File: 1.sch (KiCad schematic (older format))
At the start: 46 parts, among them J1 Micro_SD_Card, J10 BxI2C1, J11 I2C2, J2 USB_B_Micro, J3 Power, J4 SWD, J5 Protected, J6 SPI1, J7 ADC, J8 UART1, J9 SPI2, K1 NRST, K2 WKUP, K3 KPA0, U1 STM32F103C8Tx, U2 AMS1117-3.3, Y1 8MHz, Y2 32.768k

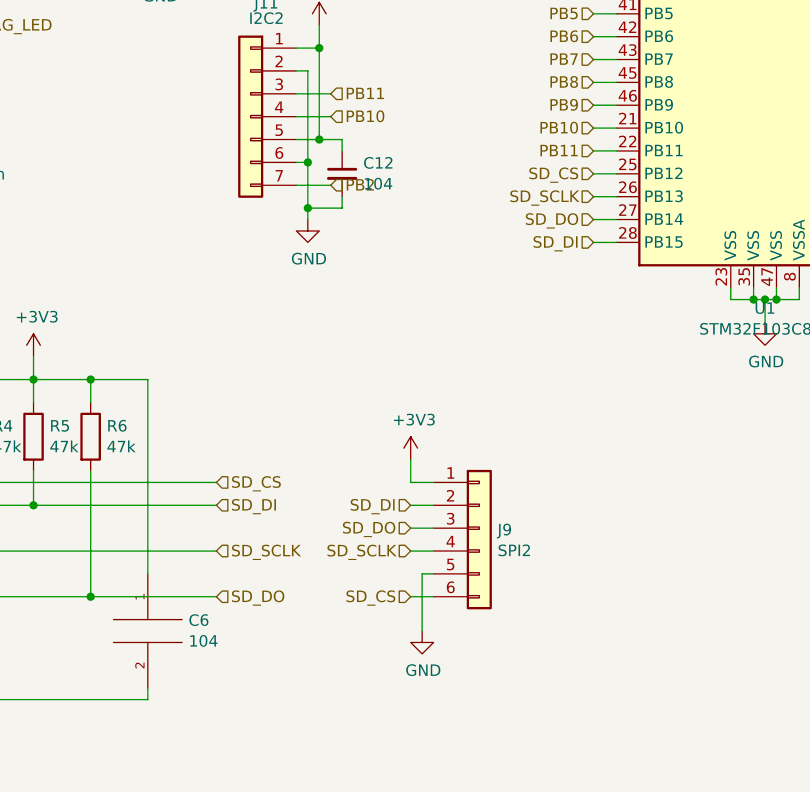
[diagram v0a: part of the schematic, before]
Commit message: rename label to PAxx/PBxx on 原理图
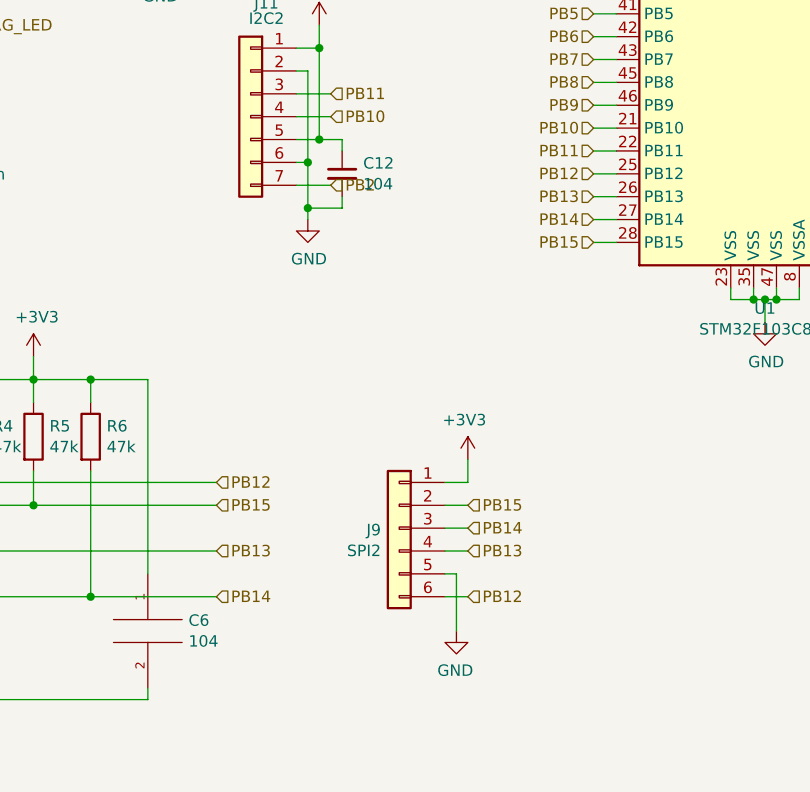
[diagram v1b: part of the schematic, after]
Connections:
- net SD_CS renamed PB12
- net SD_DI renamed PB15
- net SD_DO renamed PB14
- net SD_SCLK renamed PB13
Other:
- moved on the sheet: J9
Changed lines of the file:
@@
 	3000 6600 3800 6600
 Text HLabel 3800 6500 2    50   Input ~ 0
-SD_CS
+PB12
 Text HLabel 3800 6600 2    50   Input ~ 0
-SD_DI
+PB15
 Text HLabel 3800 6800 2    50   Input ~ 0
-SD_SCLK
+PB13
 Text HLabel 3800 7000 2    50   Input ~ 0
-SD_DO
+PB14
 $Comp
 L power:+3V3 #PWR0106
@@
 Wire Wire Line
 	5450 5150 5550 5150
-Text HLabel 5450 5250 0    50   Input ~ 0
-SD_SCLK
 Wire Wire Line
 	5450 5250 5550 5250
-Text HLabel 5450 5150 0    50   Input ~ 0
-SD_CS
 Wire Wire Line
 	5550 5350 5450 5350
@@
 	5450 5450 5550 5450
 Text HLabel 5450 5350 0    50   Input ~ 0
-SD_DO
+PB14
 Text HLabel 5450 5450 0    50   Input ~ 0
-SD_DI
+PB15
 Text HLabel 5450 2850 0    50   Input ~ 0
 NRST
@@
 	6950 2600 6950 2750
 Connection ~ 6450 2600
-Text HLabel 2750 4500 2    50   Input ~ 0
-RG_LED
 Wire Wire Line
 	10400 2700 10600 2700
@@
 L power:+3V3 #PWR0120
 U 1 1 61290385
-P 4650 6400
-F 0 "#PWR0120" H 4650 6250 50  0001 C CNN
-F 1 "+3V3" H 4665 6573 50  0000 C CNN
-F 2 "" H 4650 6400 50  0001 C CNN
-F 3 "" H 4650 6400 50  0001 C CNN
-	1    4650 6400
-	1    0    0    -1
-$EndComp
-Text HLabel 4650 7000 0    50   Input ~ 0
-SD_CS
-Wire Wire Line
-	4650 6500 4750 6500
-Wire Wire Line
-	4650 6400 4650 6500
-Wire Wire Line
-	4650 6600 4750 6600
-Wire Wire Line
-	4650 6700 4750 6700
-Wire Wire Line
-	4650 6800 4750 6800
-Text HLabel 4650 6600 0    50   Input ~ 0
-SD_DI
-Text HLabel 4650 6700 0    50   Input ~ 0
-SD_DO
-Text HLabel 4650 6800 0    50   Input ~ 0
-SD_SCLK
-Wire Wire Line
-	4700 6900 4700 7150
+P 4900 6400
+F 0 "#PWR0120" H 4900 6250 50  0001 C CNN
+F 1 "+3V3" H 4915 6573 50  0000 C CNN
+F 2 "" H 4900 6400 50  0001 C CNN
+F 3 "" H 4900 6400 50  0001 C CNN
+	1    4900 6400
+	-1   0    0    -1
+$EndComp
+Text HLabel 4900 7000 2    50   Input ~ 0
+PB12
+Wire Wire Line
+	4900 6500 4800 6500
+Wire Wire Line
+	4900 6400 4900 6500
+Wire Wire Line
+	4900 6600 4800 6600
+Wire Wire Line
+	4900 6700 4800 6700
+Wire Wire Line
+	4900 6800 4800 6800
+Text HLabel 4900 6600 2    50   Input ~ 0
+PB15
+Text HLabel 4900 6700 2    50   Input ~ 0
+PB14
+Text HLabel 4900 6800 2    50   Input ~ 0
+PB13
+Wire Wire Line
+	4850 6900 4850 7150
 $Comp
 L power:GND #PWR0124
 U 1 1 61009CA8
-P 4700 7150
-F 0 "#PWR0124" H 4700 6900 50  0001 C CNN
-F 1 "GND" H 4705 6977 50  0000 C CNN
-F 2 "" H 4700 7150 50  0001 C CNN
-F 3 "" H 4700 7150 50  0001 C CNN
-	1    4700 7150
-	1    0    0    -1
-$EndComp
-Wire Wire Line
-	4750 6900 4700 6900
-Wire Wire Line
-	4650 7000 4750 7000
+P 4850 7150
+F 0 "#PWR0124" H 4850 6900 50  0001 C CNN
+F 1 "GND" H 4855 6977 50  0000 C CNN
+F 2 "" H 4850 7150 50  0001 C CNN
+F 3 "" H 4850 7150 50  0001 C CNN
+	1    4850 7150
+	-1   0    0    -1
+$EndComp
+Wire Wire Line
+	4800 6900 4850 6900
+Wire Wire Line
+	4900 7000 4800 7000
 $Comp
 L Connector_Generic:Conn_01x06 J9
 U 1 1 61009C91
-P 4950 6700
-F 0 "J9" H 5030 6692 50  0000 L CNN
-F 1 "SPI2" H 5030 6601 50  0000 L CNN
-F 2 "Connector_PinHeader_2.54mm:PinHeader_1x06_P2.54mm_Vertical" H 5030 6555 50  0001 L CNN
-F 3 "~" H 4950 6700 50  0001 C CNN
-	1    4950 6700
-	1    0    0    -1
+P 4600 6700
+F 0 "J9" H 4680 6692 50  0000 L CNN
+F 1 "SPI2" H 4680 6601 50  0000 L CNN
+F 2 "Connector_PinHeader_2.54mm:PinHeader_1x06_P2.54mm_Vertical" H 4680 6555 50  0001 L CNN
+F 3 "~" H 4600 6700 50  0001 C CNN
+	1    4600 6700
+	-1   0    0    -1
 $EndComp
 Connection ~ 4200 5300
@@
 Text HLabel 4300 4900 2    50   Input ~ 0
 PB10
+Text HLabel 5450 5250 0    50   Input ~ 0
+PB13
+Text HLabel 5450 5150 0    50   Input ~ 0
+PB12
+Text HLabel 2750 4500 2    50   Input ~ 0
+RG_LED
 $EndSCHEMATC

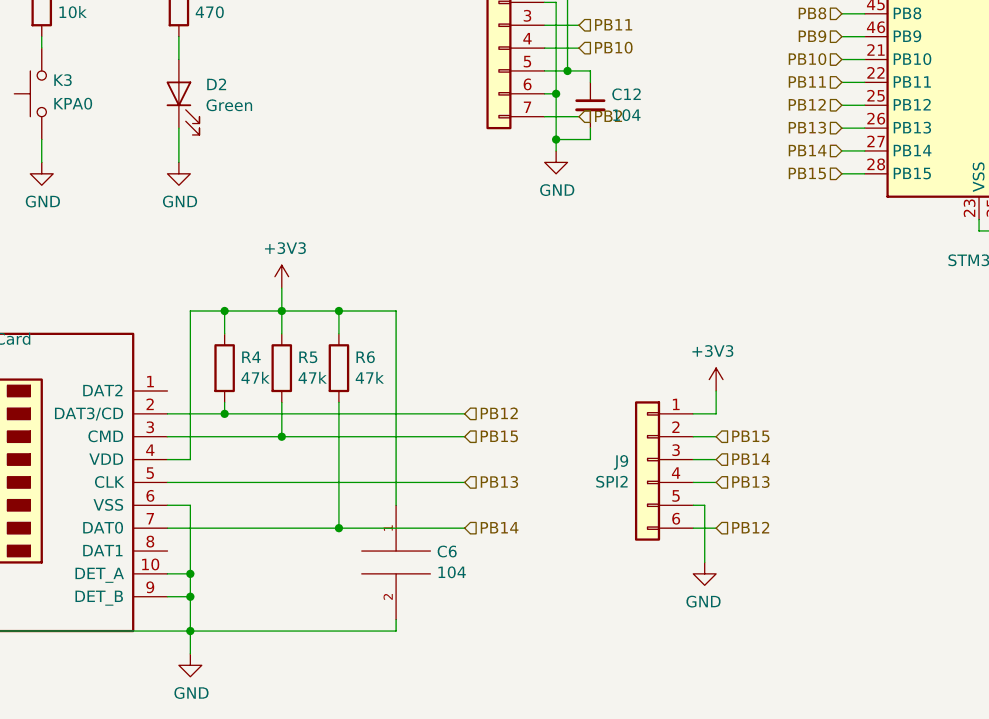
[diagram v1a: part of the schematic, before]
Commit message: 添加不连接标签
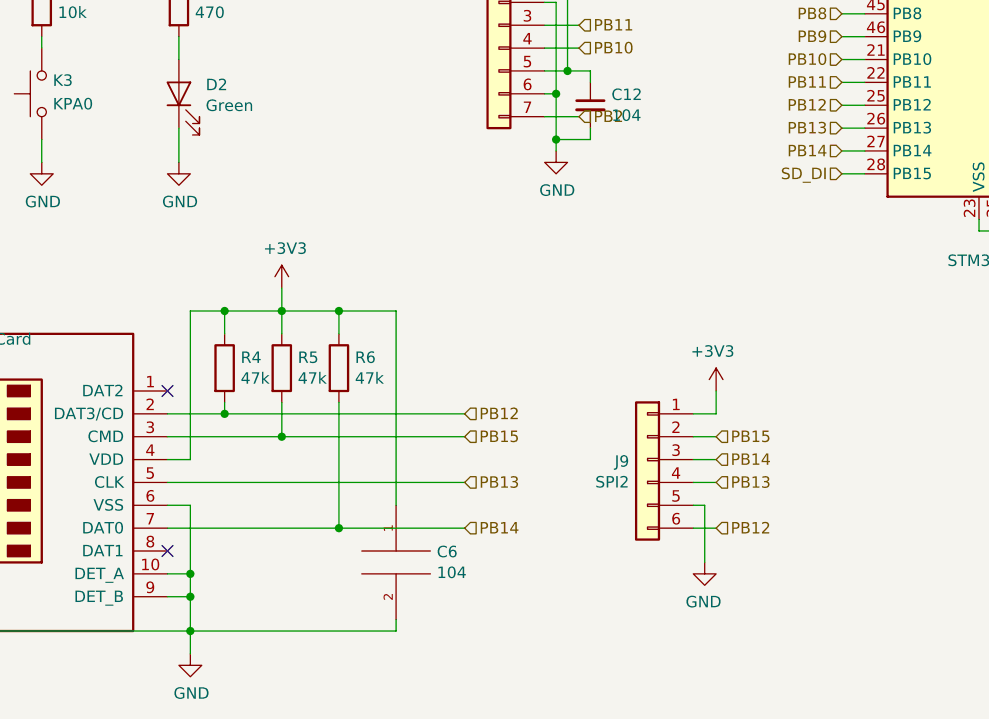
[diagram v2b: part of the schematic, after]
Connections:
- net PB15: no longer U1.28 (PB15)
- new net SD_DI: U1.28 (PB15)
- no-connect marks 0 -> 2
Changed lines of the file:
@@
 Text HLabel 5450 5350 0    50   Input ~ 0
 PB14
-Text HLabel 5450 5450 0    50   Input ~ 0
-PB15
 Text HLabel 5450 2850 0    50   Input ~ 0
 NRST
@@
 Text HLabel 2750 4500 2    50   Input ~ 0
 RG_LED
+Text HLabel 5450 5450 0    50   Input ~ 0
+SD_DI
+NoConn ~ 2500 6400
+NoConn ~ 2500 7100
 $EndSCHEMATC

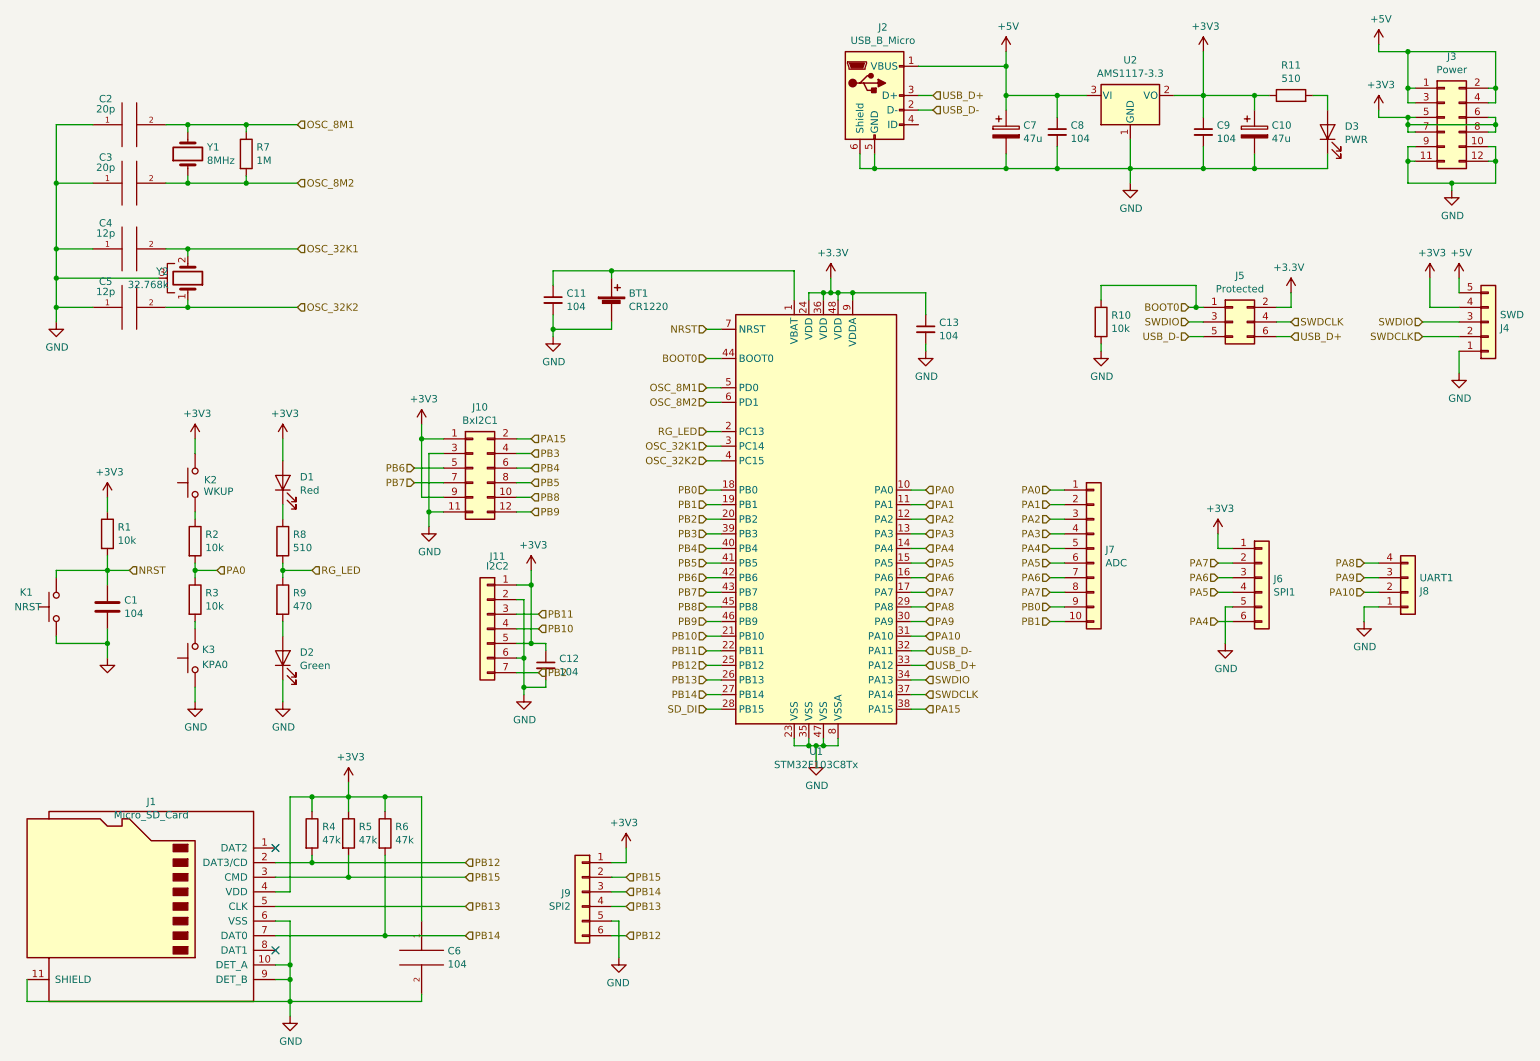
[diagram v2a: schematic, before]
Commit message: 使用网络标签代替层次标签
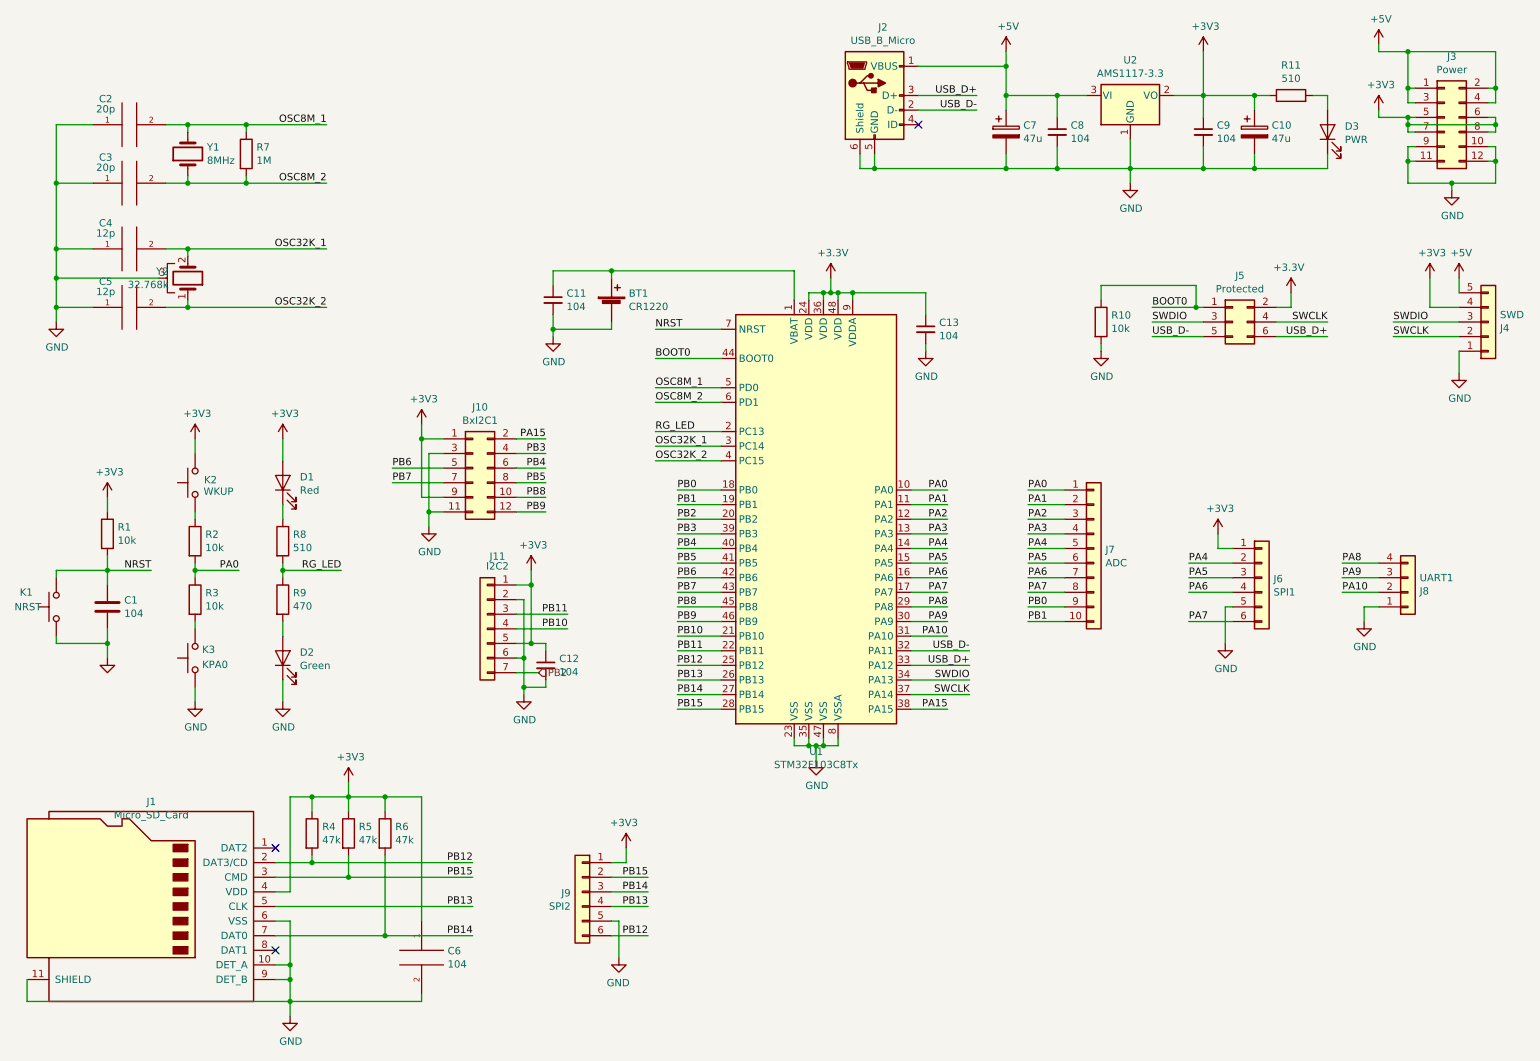
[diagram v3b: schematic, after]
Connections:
- net SD_DI is gone; now on net PB15: U1.28 (PB15)
- net PA4: now also J6.2 (Pin_2); no longer J6.6 (Pin_6)
- net PA5: now also J6.3 (Pin_3); no longer J6.4 (Pin_4)
- net PA6: now also J6.4 (Pin_4); no longer J6.3 (Pin_3)
- net PA7: now also J6.6 (Pin_6); no longer J6.2 (Pin_2)
- net OSC_32K1 renamed OSC32K_1
- net OSC_32K2 renamed OSC32K_2
- net OSC_8M1 renamed OSC8M_1
- net OSC_8M2 renamed OSC8M_2
- net SWDCLK renamed SWCLK
- no-connect marks 2 -> 3
